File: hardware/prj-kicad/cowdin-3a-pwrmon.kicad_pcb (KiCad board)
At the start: 4 copper layers, 50 x 86.5 mm, 2 parts, among them P1 CONN_9, P2 CONN_9

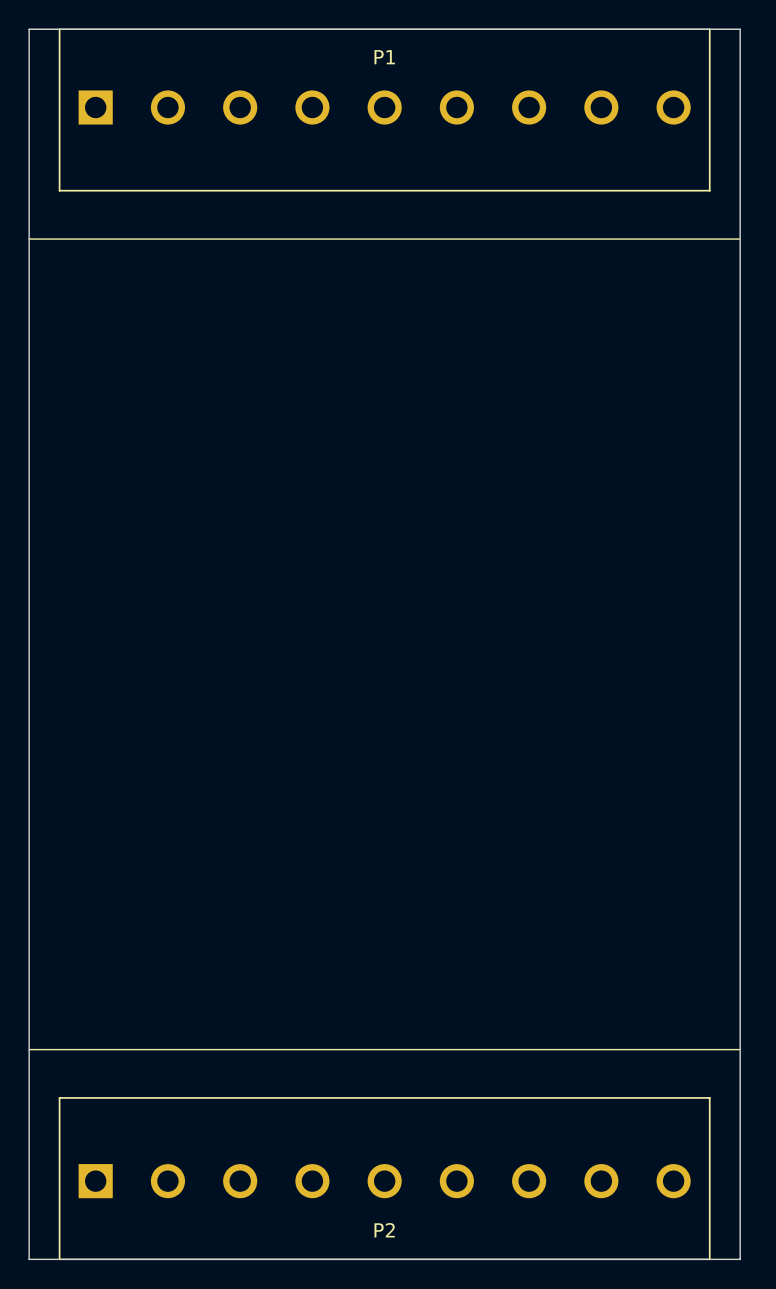
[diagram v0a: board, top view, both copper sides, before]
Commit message: Hardware: Add communication interfaces (RS485 and Linky)
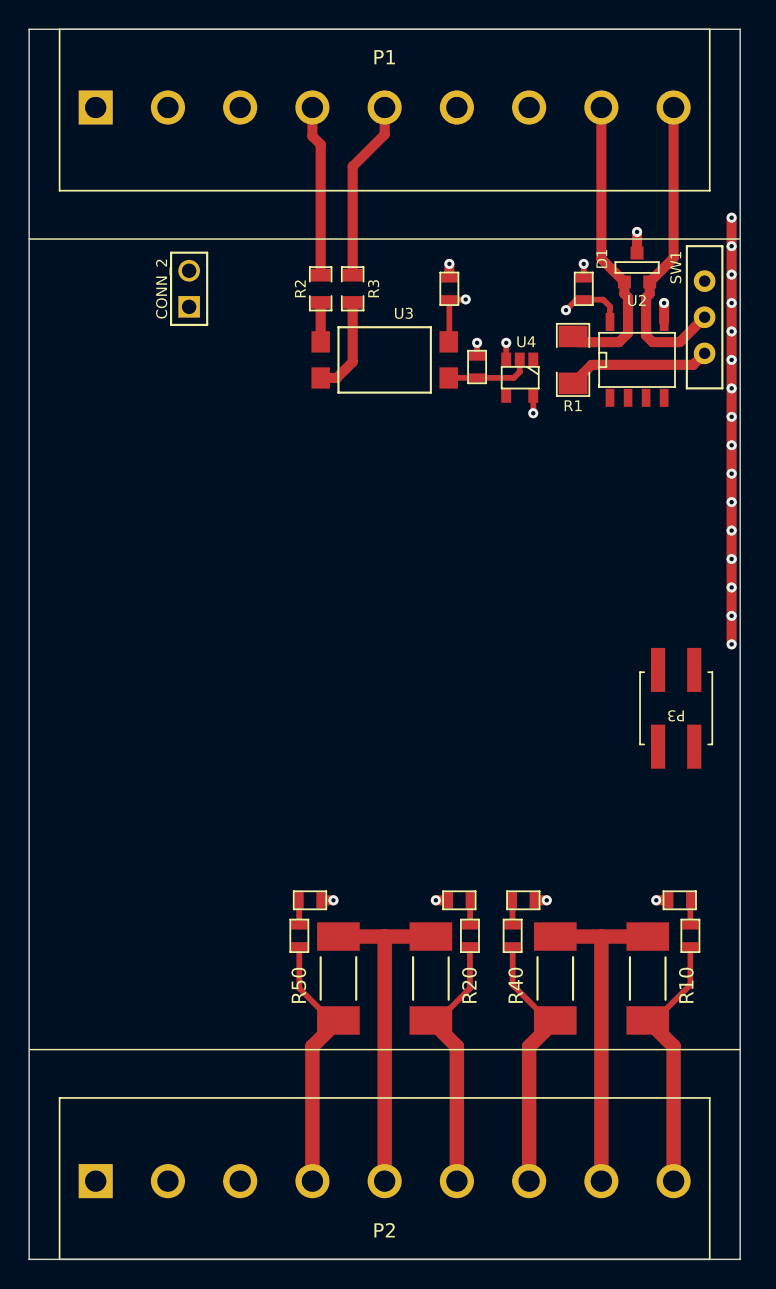
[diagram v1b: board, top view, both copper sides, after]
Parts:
- added C10: 100nF, cowdin-3a-pwrmon:SMD0603, F.Cu at (162.5, 80.0)
- added C11: 100nF, cowdin-3a-pwrmon:SMD0603, F.Cu at (153.1, 80.0)
- added CONN_2: Val**, cowdin-3a-pwrmon:CONN_2, F.Cu at (134.8, 80.0)
- added D1: SM712, cowdin-3a-pwrmon:SOT23-3, F.Cu at (166.2, 78.5)
- added P3: CONN_2x2, cowdin-3a-pwrmon:CONN_SMD2x2, F.Cu at (169.0, 109.5)
- added R1: 120, cowdin-3a-pwrmon:SMD1206, F.Cu at (161.8, 85.0)
- added R10: 33, cowdin-3a-pwrmon:SMD2010, F.Cu at (167.0, 128.5)
- added R11: 0, cowdin-3a-pwrmon:SMD0603, F.Cu at (170.0, 125.5)
- added R12: n/e, cowdin-3a-pwrmon:SMD0603, F.Cu at (169.2, 123.0)
- added R2: 2,4k, cowdin-3a-pwrmon:SMD0805, F.Cu at (144.0, 80.0)
- added R20: 33, cowdin-3a-pwrmon:SMD2010, F.Cu at (151.8, 128.5)
- added R21: 0, cowdin-3a-pwrmon:SMD0603, F.Cu at (154.5, 125.5)
- added R22: n/e, cowdin-3a-pwrmon:SMD0603, F.Cu at (153.8, 123.0)
- added R3: 2,4k, cowdin-3a-pwrmon:SMD0805, F.Cu at (146.2, 80.0)
- added R4: 10k, cowdin-3a-pwrmon:SMD0603, F.Cu at (155.0, 85.5)
- added R40: 33, cowdin-3a-pwrmon:SMD2010, F.Cu at (160.5, 128.5)
- added R41: 0, cowdin-3a-pwrmon:SMD0603, F.Cu at (157.5, 125.5)
- added R42: n/e, cowdin-3a-pwrmon:SMD0603, F.Cu at (158.2, 123.0)
- added R50: 33, cowdin-3a-pwrmon:SMD2010, F.Cu at (145.2, 128.5)
- added R52: 0, cowdin-3a-pwrmon:SMD0603, F.Cu at (142.5, 125.5)
- added R53: n/e, cowdin-3a-pwrmon:SMD0603, F.Cu at (143.2, 123.0)
- added SW1: JUMPER, cowdin-3a-pwrmon:SW_450301014042, F.Cu at (171.0, 82.0)
- added U2: SN65HVD72, cowdin-3a-pwrmon:SOIC-8E, F.Cu at (166.2, 85.0)
- added U3: LTV814, cowdin-3a-pwrmon:SMD4, F.Cu at (148.5, 85.0)
- added U4: SN74LVC1G14, cowdin-3a-pwrmon:SOT23-5, F.Cu at (158.0, 86.2)
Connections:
- P1 pad 8: RS485_A -> RS485_B
- P1 pad 9: RS485_B -> RS485_A
- P2 pad 4: unconnected-(P2-Pad4) -> CT5_A
- P2 pad 5: unconnected-(P2-Pad5) -> CT2_B
- P2 pad 6: unconnected-(P2-Pad6) -> CT2_A
- P2 pad 7: unconnected-(P2-Pad7) -> CT4_A
- P2 pad 8: unconnected-(P2-Pad8) -> CT1_B
- P2 pad 9: unconnected-(P2-Pad9) -> CT1_A
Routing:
- net GND: track 0.00 -> 129.7 mm, vias 0 -> 26
- net +5V: track 0.00 -> 29.5 mm, vias 0 -> 3
- net CT1_B: track 0.00 -> 23.7 mm
- net CT2_B: track 0.00 -> 23.7 mm
- net RS485_A: track 0.00 -> 21.9 mm
- net RS485_B: track 0.00 -> 20.9 mm
- net CT4_A: track 0.00 -> 18.8 mm
- net CT1_A: track 0.00 -> 18.8 mm
- net CT5_A: track 0.00 -> 18.7 mm
- net CT2_A: track 0.00 -> 18.7 mm
- net LINKY_I2: track 0.00 -> 12.7 mm
- net LINKY_I1: track 0.00 -> 12.0 mm
- net Net-(R1-Pad1): track 0.00 -> 10.1 mm
- net Net-(R3-Pad1): track 0.00 -> 6.91 mm
- net Net-(R4-Pad1): track 0.00 -> 6.04 mm
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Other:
- board text added: "Fix"

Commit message: Hardware: Add power supply
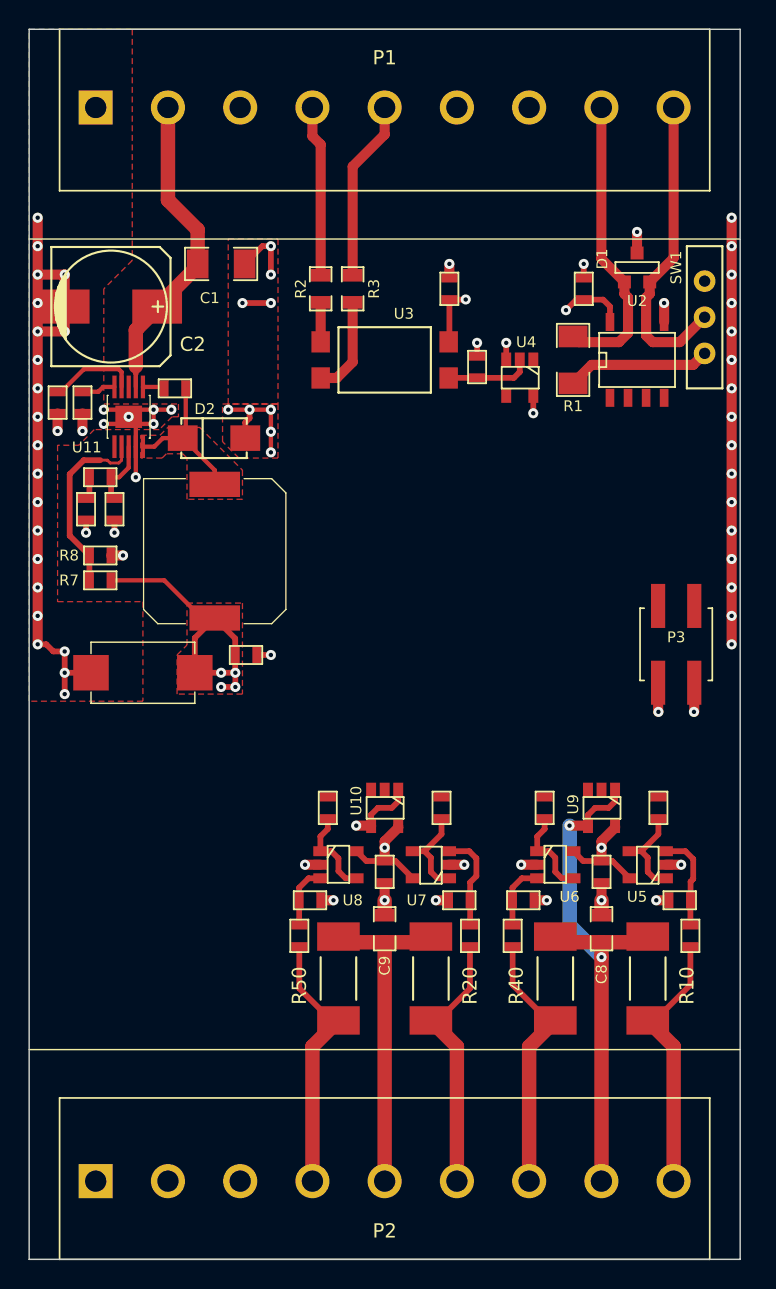
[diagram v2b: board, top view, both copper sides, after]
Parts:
- removed CONN_2: Val**, cowdin-3a-pwrmon:CONN_2
- added C1: 2,2uF, cowdin-3a-pwrmon:SMD1206, F.Cu at (137.0, 78.2)
- added C12: 100nF, cowdin-3a-pwrmon:SMD0603, F.Cu at (133.8, 87.0)
- added C13: 1uF, cowdin-3a-pwrmon:SMD0603, F.Cu at (138.8, 105.8)
- added C14: 220uF, cowdin-3a-pwrmon:C_TPB_D4, F.Cu at (131.5, 107.0)
- added C2: 100uF, cowdin-3a-pwrmon:C_ALU_8x10.5, F.Cu at (129.2, 81.2)
- added C3: 10nF, cowdin-3a-pwrmon:SMD0603, F.Cu at (125.5, 88.0)
- added C4: n/a, cowdin-3a-pwrmon:SMD0603, F.Cu at (129.5, 95.5)
- added C5: 4,7nF, cowdin-3a-pwrmon:SMD0603, F.Cu at (127.5, 95.5)
- added C6: 100nF, cowdin-3a-pwrmon:SMD0603, F.Cu at (148.5, 121.0)
- added C7: 100nF, cowdin-3a-pwrmon:SMD0603, F.Cu at (163.8, 121.0)
- added C8: 4,7uF, cowdin-3a-pwrmon:SMD0805, F.Cu at (163.8, 125.0)
- added C9: 4,7uF, cowdin-3a-pwrmon:SMD0805, F.Cu at (148.5, 125.0)
- added D2: MBRA340, cowdin-3a-pwrmon:DO214AC, F.Cu at (136.5, 90.5)
- added L1: 27uH, cowdin-3a-pwrmon:I_MSS1048, F.Cu at (136.6, 98.5)
- added R13: 0, cowdin-3a-pwrmon:SMD0603, F.Cu at (167.8, 116.5)
- added R23: 0, cowdin-3a-pwrmon:SMD0603, F.Cu at (152.5, 116.5)
- added R43: 0, cowdin-3a-pwrmon:SMD0603, F.Cu at (159.8, 116.5)
- added R5: 100k, cowdin-3a-pwrmon:SMD0603, F.Cu at (127.2, 88.0)
- added R53: 0, cowdin-3a-pwrmon:SMD0603, F.Cu at (144.5, 116.5)
- added R6: 20k, cowdin-3a-pwrmon:SMD0603, F.Cu at (128.5, 93.2)
- added R7: 52,3k, cowdin-3a-pwrmon:SMD0603, F.Cu at (128.5, 100.5)
- added R8: 10k, cowdin-3a-pwrmon:SMD0603, F.Cu at (128.5, 98.8)
- added U10: MCP6001, cowdin-3a-pwrmon:SOT23-5, F.Cu at (148.5, 116.5)
- added U11: TPS54060A, cowdin-3a-pwrmon:MSOP10p, F.Cu at (130.5, 89.0)
- added U5: MCP6001, cowdin-3a-pwrmon:SOT23-5, F.Cu at (167.0, 120.5)
- added U6: MCP6001, cowdin-3a-pwrmon:SOT23-5, F.Cu at (160.5, 120.5)
- added U7: MCP6001, cowdin-3a-pwrmon:SOT23-5, F.Cu at (151.8, 120.5)
- added U8: MCP6001, cowdin-3a-pwrmon:SOT23-5, F.Cu at (145.2, 120.5)
- added U9: MCP6001, cowdin-3a-pwrmon:SOT23-5, F.Cu at (163.8, 116.5)
- moved P3 4.50 mm to (169.0, 105.0), turned to 0 degrees
- renumbered R52 to R51, R53 to R52
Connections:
- P1 pad 1: VIN- -> GND
- P1 pad 2: VIN+ -> +VIn
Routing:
- net GND: track 129.7 -> 341.5 mm, vias 26 -> 76
- net +5V: track 29.5 -> 142.9 mm, vias 3 -> 10
- net +VIn: track 0.00 -> 22.3 mm
- net CT1_B: track 23.7 -> 39.0 mm, vias 0 -> 2
- net Net-(R7-Pad1): track 0.00 -> 13.2 mm
- net /Power Supply/V5_SW: track 0.00 -> 10.8 mm
- net Net-(R13-Pad2): track 0.00 -> 6.70 mm
- net Net-(R23-Pad2): track 0.00 -> 6.70 mm
- net Net-(R43-Pad2): track 0.00 -> 6.42 mm
- net Net-(R53-Pad2): track 0.00 -> 6.36 mm
- net Net-(C3-Pad1): track 0.00 -> 6.29 mm
- net Net-(R21-Pad1): track 1.74 -> 7.01 mm
- net Net-(R11-Pad1): track 1.74 -> 6.88 mm
- net CT2_B: track 23.7 -> 28.6 mm, vias 0 -> 1
- net Net-(C4-Pad1): track 0.00 -> 4.58 mm
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- added copper zone on F.Cu, net +5V
- added copper zone on F.Cu, net /Power Supply/V5_SW
- added copper zone on F.Cu, net GND
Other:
- board text removed: "CT_02"
- board text removed: "POWER"

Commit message: Hardware: Add processor (ATMSAMC21) and relay option
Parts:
- added C15: 100nF, cowdin-3a-pwrmon:SMD0603, F.Cu at (164.5, 99.8)
- added C16: 100nF, cowdin-3a-pwrmon:SMD0603, F.Cu at (159.8, 89.7)
- added C17: 100nF, cowdin-3a-pwrmon:SMD0603, F.Cu at (151.0, 89.5)
- added C18: 100nF, cowdin-3a-pwrmon:SMD0603, F.Cu at (147.0, 96.8)
- added C19: 100nF, cowdin-3a-pwrmon:SMD0603, F.Cu at (147.0, 98.2)
- added C20: 100nF, cowdin-3a-pwrmon:SMD0603, F.Cu at (156.0, 106.7)
- added C21: 1uF, cowdin-3a-pwrmon:SMD0603, F.Cu at (131.8, 105.5)
- added C22: 1uF, cowdin-3a-pwrmon:SMD0603, F.Cu at (147.0, 95.0)
- added D3: D, cowdin-3a-pwrmon:SOD-123, F.Cu at (131.8, 110.0)
- added Q1: Si2318, cowdin-3a-pwrmon:SOT23-3, F.Cu at (136.5, 117.8)
- added R14: 10k, cowdin-3a-pwrmon:SMD0603, F.Cu at (147.0, 91.5)
- added R9: 10k, cowdin-3a-pwrmon:SMD0603, F.Cu at (147.0, 93.2)
- added RL1: RELAY, cowdin-3a-pwrmon:RL_3451, F.Cu at (128.7, 105.6)
- added U1: ATSAMC21J, cowdin-3a-pwrmon:TQFP64, F.Cu at (155.5, 98.0)
- moved P3 7.00 mm to (169.0, 98.0)
- moved C14 5.32 mm to (135.5, 110.5), turned to -90 degrees
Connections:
- P2 pad 1: unconnected-(P2-Pad1) -> RL_NO
- P2 pad 2: unconnected-(P2-Pad2) -> RL_COM
- P2 pad 3: unconnected-(P2-Pad3) -> RL_NC
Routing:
- net GND: track 341.5 -> 498.5 mm, vias 76 -> 119
- net +5V: track 142.9 -> 231.3 mm, vias 10 -> 17
- net RL_NC: track 0.00 -> 26.1 mm
- net RL_COM: track 0.00 -> 19.0 mm
- net EXT_RX: track 0.00 -> 12.8 mm
- net Net-(D3-Pad1): track 0.00 -> 12.5 mm
- net RL_NO: track 0.00 -> 12.4 mm
- net RS485_DIR: track 0.00 -> 12.2 mm
- net RS485_TX: track 0.00 -> 12.0 mm
- net SWCLK: track 0.00 -> 11.0 mm
- net RS485_RX: track 0.00 -> 10.5 mm
- net CT2_B: track 28.6 -> 38.7 mm, vias 1 -> 2
- net EXT_TX: track 0.00 -> 7.33 mm
- net LINKY_RX: track 0.00 -> 4.86 mm
- net RST: track 0.00 -> 4.04 mm
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- added copper zone on In2.Cu, net +5V
- added copper zone on In1.Cu, net GND
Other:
- board text removed: "MCU"

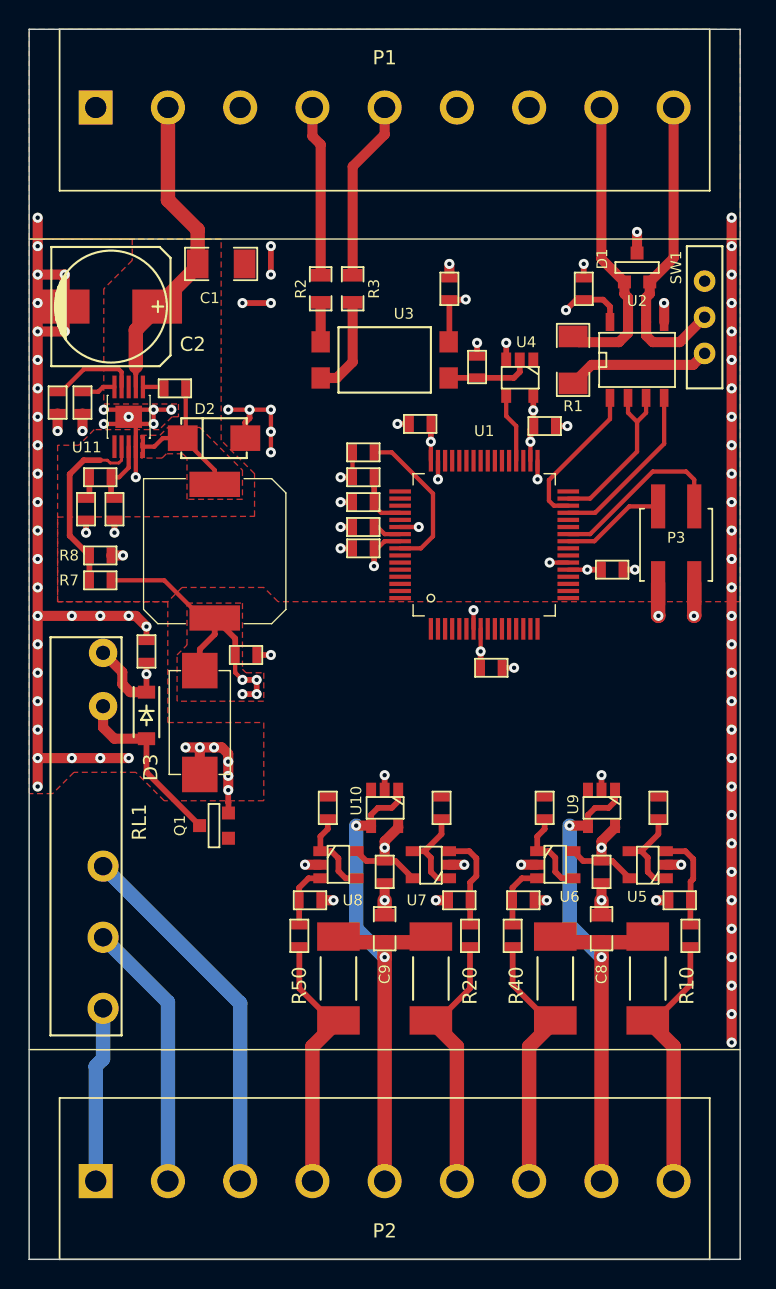
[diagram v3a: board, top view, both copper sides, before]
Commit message: Hardware: Finish current sensor interface and create production files for rev1
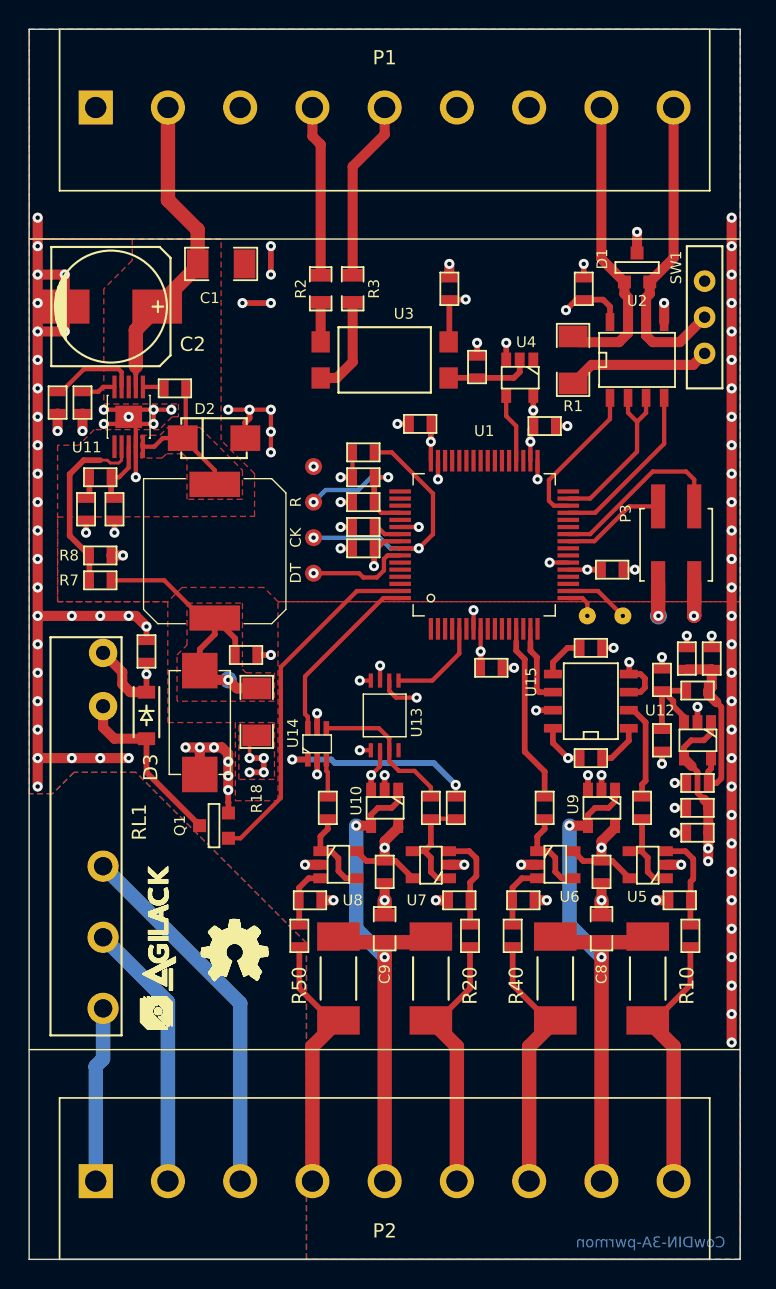
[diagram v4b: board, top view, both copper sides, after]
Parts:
- added C23: 1uF, cowdin-3a-pwrmon:SMD0603, F.Cu at (170.5, 116.5)
- added C24: 470pF, cowdin-3a-pwrmon:SMD0603, F.Cu at (170.5, 118.2)
- added C25: 100nF, cowdin-3a-pwrmon:SMD0603, F.Cu at (171.5, 106.0)
- added C26: 470pF, cowdin-3a-pwrmon:SMD0603, F.Cu at (170.5, 114.8)
- added C27: 470pF, cowdin-3a-pwrmon:SMD0603, F.Cu at (168.0, 107.5)
- added C28: C, cowdin-3a-pwrmon:SMD0603, F.Cu at (163.0, 105.2)
- added C29: C, cowdin-3a-pwrmon:SMD0603, F.Cu at (163.0, 113.0)
- added L2: FB100, cowdin-3a-pwrmon:SMD0603, F.Cu at (169.8, 106.0)
- added R15: 10k, cowdin-3a-pwrmon:SMD0603, F.Cu at (170.5, 108.2)
- added R16: 10k, cowdin-3a-pwrmon:SMD0603, F.Cu at (168.0, 111.8)
- added R17: 0, cowdin-3a-pwrmon:SMD0603, F.Cu at (151.8, 116.5)
- added R18: 0, cowdin-3a-pwrmon:SMD1206, F.Cu at (139.5, 109.8)
- added TP1: CONN_1, cowdin-3a-pwrmon:TP_SMD, B.Cu at (167.8, 103.0)
- added TP2: CONN_1, cowdin-3a-pwrmon:TP_SMD, B.Cu at (137.5, 107.5)
- added TP3: CONN_1, cowdin-3a-pwrmon:TP_SMD, F.Cu at (143.5, 97.5)
- added TP4: CONN_1, cowdin-3a-pwrmon:TP_SMD, F.Cu at (143.5, 100.0)
- added TP5: CONN_1, cowdin-3a-pwrmon:TP_SMD, F.Cu at (143.5, 95.0)
- added TP6: CONN_1, cowdin-3a-pwrmon:TP_SMD, F.Cu at (143.5, 92.5)
- added TP7: CONN_1, cowdin-3a-pwrmon:TP_2SMD, F.Cu at (162.8, 103.0)
- added TP8: CONN_1, cowdin-3a-pwrmon:TP_2SMD, F.Cu at (165.2, 103.0)
- added U12: MCP6001, cowdin-3a-pwrmon:SOT23-5, F.Cu at (170.5, 111.8)
- added U13: LTC1968, cowdin-3a-pwrmon:MSOP-8, F.Cu at (148.5, 110.0)
- added U14: SN74LVC1G3157, cowdin-3a-pwrmon:SC70-6, F.Cu at (143.8, 112.0)
- added U15: AD737, cowdin-3a-pwrmon:SOIC-8E, F.Cu at (163.0, 109.0)
- added agilack-11.5: 450px, cowdin-3a-pwrmon:logo-agilack-11.5, F.Cu at (132.6, 126.0)
- added ohw_logo: VAL**, cowdin-3a-pwrmon:logo-ohw, F.Cu at (137.9, 126.7)
- moved R13 1.15 mm to (166.6, 116.5)
- moved R23 1.00 mm to (153.5, 116.5)
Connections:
- C13 pad 1: +5V -> /Power Supply/5V_RAW
- C14 pad 1: +5V -> /Power Supply/5V_RAW
- L1 pad 2: +5V -> /Power Supply/5V_RAW
- R23 pad 1: CT2_I -> Net-(R23-Pad1)
- R23 pad 2: Net-(R23-Pad2) -> CT2_I
- R7 pad 2: +5V -> /Power Supply/5V_RAW
- U1 pad 13: unconnected-(U1-Pad13) -> CT4_I
- U1 pad 15: unconnected-(U1-Pad15) -> CT1_OUT
- U1 pad 17: unconnected-(U1-Pad17) -> Net-(TP7-Pad1)
- U1 pad 18: unconnected-(U1-Pad18) -> Net-(TP8-Pad1)
- U1 pad 5: unconnected-(U1-Pad5) -> CT2_OUT
- U1 pad 63: unconnected-(U1-Pad63) -> RELAY
- U1 pad 64: unconnected-(U1-Pad64) -> CT_SEL1
- U7 pad 1: Net-(R23-Pad2) -> CT2_I
- U7 pad 4: Net-(R23-Pad2) -> CT2_I
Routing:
- net +2.5V: track 0.00 -> 43.7 mm, vias 0 -> 4
- net GND: track 498.5 -> 542.1 mm, vias 119 -> 134
- net RELAY: track 0.00 -> 24.7 mm
- net /Power Supply/5V_RAW: track 0.00 -> 20.2 mm, vias 0 -> 1
- net +5V: track 231.3 -> 215.9 mm, vias 17 -> 21
- net Net-(R23-Pad1): track 0.00 -> 14.2 mm, vias 0 -> 2
- net Net-(C25-Pad1): track 0.00 -> 12.7 mm
- net CT_SEL1: track 0.00 -> 12.7 mm
- net CT4_I: track 0.00 -> 12.7 mm
- net Net-(R17-Pad2): track 0.00 -> 10.7 mm
- net CT2_I: track 0.00 -> 8.14 mm
- net SWCLK: track 11.0 -> 18.6 mm, vias 0 -> 2
- net Net-(C27-Pad1): track 0.00 -> 7.36 mm
- net SWDAT: track 0.00 -> 7.32 mm, vias 0 -> 1
- net RST: track 4.04 -> 11.0 mm, vias 0 -> 2
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- added copper zone on In2.Cu, net +2.5V
- added copper zone on F.Cu, net /Power Supply/5V_RAW
- added copper zone on B.Cu, net GND
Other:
- board text added: "CK"
- board text added: "CowDIN-3A-pwrmon"
- board text added: "DT"
- board text added: "R"
- board text removed: "CT_01"
